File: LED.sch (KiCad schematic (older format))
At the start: 9 parts, among them U3 PCA9632DP2

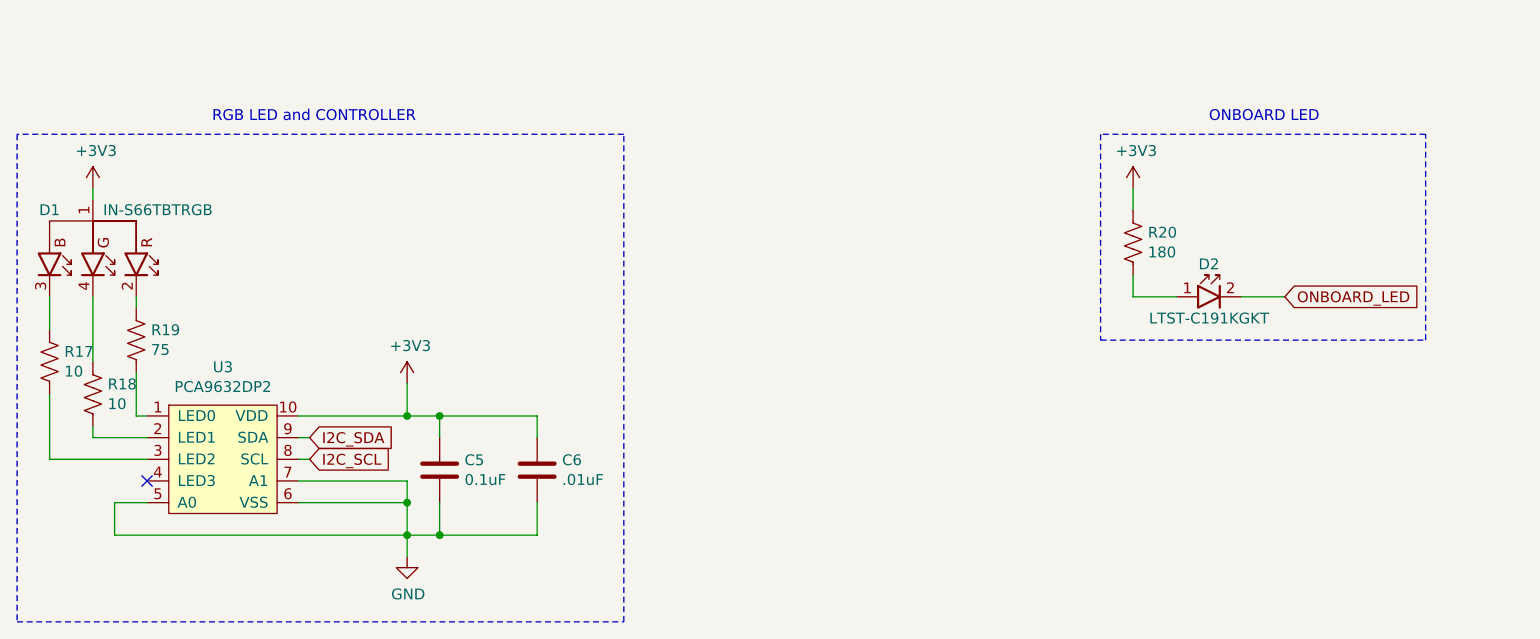
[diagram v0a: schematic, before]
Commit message: Shrink PCB, move LED to opposite corner top side
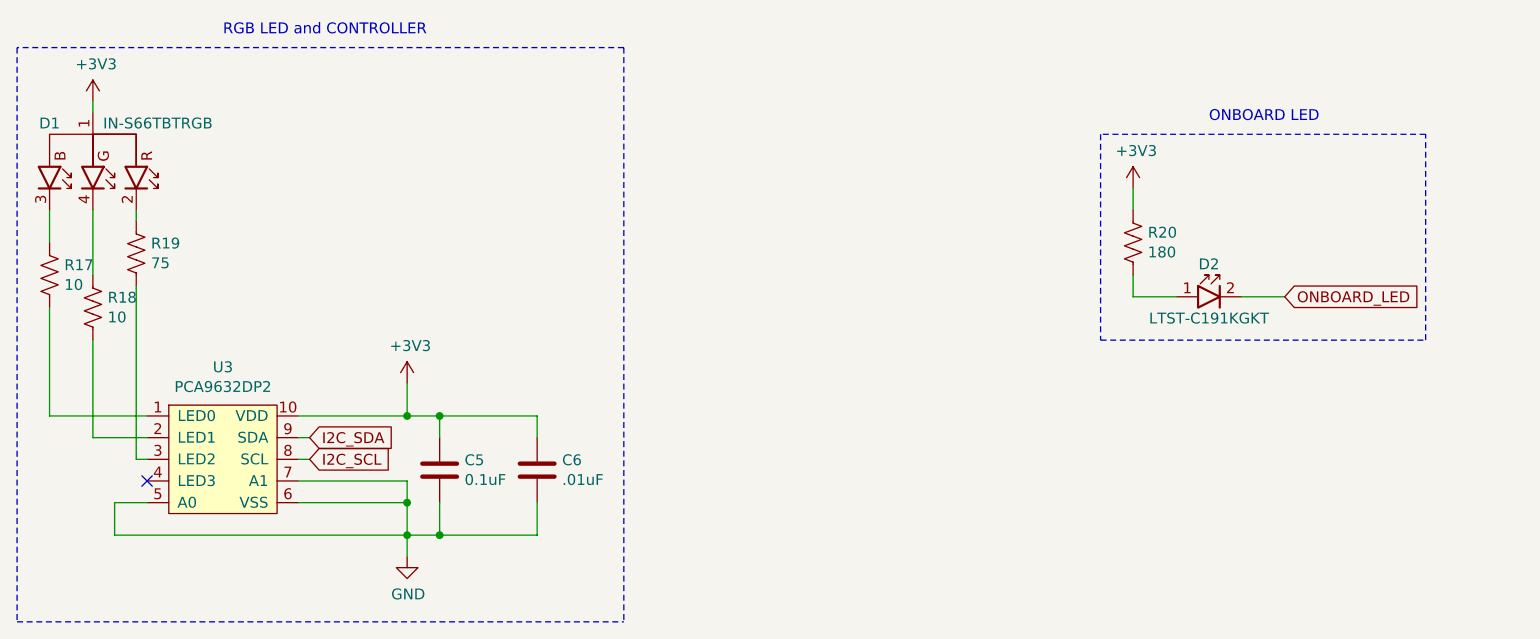
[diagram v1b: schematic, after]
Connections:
- net at U3.1 (LED0): now also R17.1; no longer R19.2
- net at U3.3 (LED2): now also R19.2; no longer R17.1
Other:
- moved on the sheet: D1, R17, R18, R19
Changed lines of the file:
@@
 L power:+3V3 #PWR?
 U 1 1 5F5452F4
-P 2650 2950
+P 2650 2550
 AR Path="/5F430268/5F431F75/5F5452F4" Ref="#PWR?"  Part="1"
 AR Path="/5F430268/5F4320C8/5F5452F4" Ref="#PWR013"  Part="1"
-F 0 "#PWR013" H 2650 2800 50  0001 C CNN
-F 1 "+3V3" H 2665 3123 50  0000 C CNN
-F 2 "" H 2650 2950 50  0001 C CNN
-F 3 "" H 2650 2950 50  0001 C CNN
-	1    2650 2950
+F 0 "#PWR013" H 2650 2400 50  0001 C CNN
+F 1 "+3V3" H 2665 2723 50  0000 C CNN
+F 2 "" H 2650 2550 50  0001 C CNN
+F 3 "" H 2650 2550 50  0001 C CNN
+	1    2650 2550
 	1    0    0    -1
 $EndComp
@@
 L Zack_Resistors:10 R17
 U 1 1 5F5480EE
-P 2450 3750
-F 0 "R17" H 2382 3704 50  0000 R CNN
-F 1 "10" H 2382 3795 50  0000 R CNN
-F 2 "Resistor_SMD:R_0603_1608Metric" V 2490 3740 50  0001 C CNN
-F 3 "~" H 2450 3750 50  0001 C CNN
-F 4 "Stackpole Electronics Inc" H 2450 3750 50  0001 C CNN "Manufacturer 1 Name"
-F 5 "RMCF0603FT10R0" H 2450 3750 50  0001 C CNN "Manufacturer 1 Part Number"
-	1    2450 3750
+P 2450 3350
+F 0 "R17" H 2382 3304 50  0000 R CNN
+F 1 "10" H 2382 3395 50  0000 R CNN
+F 2 "Resistor_SMD:R_0603_1608Metric" V 2490 3340 50  0001 C CNN
+F 3 "~" H 2450 3350 50  0001 C CNN
+F 4 "Stackpole Electronics Inc" H 2450 3350 50  0001 C CNN "Manufacturer 1 Name"
+F 5 "RMCF0603FT10R0" H 2450 3350 50  0001 C CNN "Manufacturer 1 Part Number"
+	1    2450 3350
 	-1   0    0    1
 $EndComp
@@
 L Zack_Resistors:75 R19
 U 1 1 5F548554
-P 2850 3650
-F 0 "R19" H 2918 3696 50  0000 L CNN
-F 1 "75" H 2918 3605 50  0000 L CNN
-F 2 "Resistor_SMD:R_0603_1608Metric" V 2890 3640 50  0001 C CNN
-F 3 "~" H 2850 3650 50  0001 C CNN
-F 4 "Yageo" H 2850 3650 50  0001 C CNN "Manufacturer 1 Name"
-F 5 "RC0603JR-0775RL" H 2850 3650 50  0001 C CNN "Manufacturer 1 Part Number"
-	1    2850 3650
-	1    0    0    -1
-$EndComp
-Wire Wire Line
-	2850 3500 2850 3450
-Wire Wire Line
-	2650 3450 2650 3750
-Wire Wire Line
-	2450 3450 2450 3600
-Wire Wire Line
-	2850 3800 2850 4000
-Wire Wire Line
-	2450 3900 2450 4200
-Wire Wire Line
-	2450 4200 2900 4200
+P 2850 3250
+F 0 "R19" H 2918 3296 50  0000 L CNN
+F 1 "75" H 2918 3205 50  0000 L CNN
+F 2 "Resistor_SMD:R_0603_1608Metric" V 2890 3240 50  0001 C CNN
+F 3 "~" H 2850 3250 50  0001 C CNN
+F 4 "Yageo" H 2850 3250 50  0001 C CNN "Manufacturer 1 Name"
+F 5 "RC0603JR-0775RL" H 2850 3250 50  0001 C CNN "Manufacturer 1 Part Number"
+	1    2850 3250
+	1    0    0    -1
+$EndComp
+Wire Wire Line
+	2850 3100 2850 3050
+Wire Wire Line
+	2650 3050 2650 3350
+Wire Wire Line
+	2450 3050 2450 3200
 NoConn ~ 2900 4300
 Wire Wire Line
@@
 	3600 4000 4100 4000
 Wire Wire Line
-	2650 2950 2650 3000
+	2650 2550 2650 2600
 $Comp
 L power:+3V3 #PWR?
@@
 Connection ~ 4100 4400
 Wire Wire Line
-	2900 4400 2750 4400
-Wire Wire Line
 	2750 4400 2750 4550
 Wire Wire Line
@@
 	4100 4550 4100 4650
 $Comp
-L Zack_Diodes:IN-S66TBTRGB D1
-U 1 1 5F546435
-P 2650 3200
-F 0 "D1" V 2500 3000 50  0000 C CNN
-F 1 "IN-S66TBTRGB" V 2500 3500 50  0000 C CNN
-F 2 "Zack_Diodes:0606_1616Metric" H 4129 4004 50  0001 C CNN
-F 3 "" H 4129 4004 50  0001 C CNN
-F 4 "Inolux" H 2650 3200 50  0001 C CNN "Manufacturer 1 Name"
-F 5 "IN-S66TBTRGB" H 2650 3200 50  0001 C CNN "Manufacturer 1 Part Number"
-	1    2650 3200
-	0    1    1    0
-$EndComp
-Wire Wire Line
-	2650 4050 2650 4100
-$Comp
 L Zack_Resistors:10 R18
 U 1 1 5F547547
-P 2650 3900
-F 0 "R18" H 2582 3854 50  0000 R CNN
-F 1 "10" H 2582 3945 50  0000 R CNN
-F 2 "Resistor_SMD:R_0603_1608Metric" V 2690 3890 50  0001 C CNN
-F 3 "~" H 2650 3900 50  0001 C CNN
-F 4 "Stackpole Electronics Inc" H 2650 3900 50  0001 C CNN "Manufacturer 1 Name"
-F 5 "RMCF0603FT10R0" H 2650 3900 50  0001 C CNN "Manufacturer 1 Part Number"
-	1    2650 3900
+P 2650 3500
+F 0 "R18" H 2582 3454 50  0000 R CNN
+F 1 "10" H 2582 3545 50  0000 R CNN
+F 2 "Resistor_SMD:R_0603_1608Metric" V 2690 3490 50  0001 C CNN
+F 3 "~" H 2650 3500 50  0001 C CNN
+F 4 "Stackpole Electronics Inc" H 2650 3500 50  0001 C CNN "Manufacturer 1 Name"
+F 5 "RMCF0603FT10R0" H 2650 3500 50  0001 C CNN "Manufacturer 1 Part Number"
+	1    2650 3500
 	-1   0    0    1
 $EndComp
-Wire Wire Line
-	2850 4000 2900 4000
 Wire Wire Line
 	2650 4100 2900 4100
@@
 ONBOARD LED
 Wire Notes Line
-	2300 2700 2300 4950
-Wire Notes Line
 	2300 4950 5100 4950
 Wire Notes Line
-	5100 4950 5100 2700
-Wire Notes Line
-	5100 2700 2300 2700
-Text Notes 3200 2650 0    50   ~ 0
+	5100 2300 2300 2300
+Text Notes 3250 2250 0    50   ~ 0
 RGB LED and CONTROLLER
+Wire Wire Line
+	2900 4400 2750 4400
+$Comp
+L Zack_Diodes:IN-S66TBTRGB D1
+U 1 1 5F546435
+P 2650 2800
+F 0 "D1" V 2500 2600 50  0000 C CNN
+F 1 "IN-S66TBTRGB" V 2500 3100 50  0000 C CNN
+F 2 "Zack_Diodes:0606_1616Metric" H 4129 3604 50  0001 C CNN
+F 3 "" H 4129 3604 50  0001 C CNN
+F 4 "Inolux" H 2650 2800 50  0001 C CNN "Manufacturer 1 Name"
+F 5 "IN-S66TBTRGB" H 2650 2800 50  0001 C CNN "Manufacturer 1 Part Number"
+	1    2650 2800
+	0    1    1    0
+$EndComp
+Wire Wire Line
+	2450 4000 2450 3500
+Wire Wire Line
+	2450 4000 2900 4000
+Wire Wire Line
+	2650 4100 2650 3650
+Wire Wire Line
+	2900 4200 2850 4200
+Wire Wire Line
+	2850 4200 2850 3400
+Wire Notes Line
+	2300 2300 2300 4950
+Wire Notes Line
+	5100 2300 5100 4950
 $EndSCHEMATC
